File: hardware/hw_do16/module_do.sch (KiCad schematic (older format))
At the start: 130 parts, among them J1 DO_0, J2 DO_1, J3 MOD, P3 DEBUG, Q1 IRLML5103, Q10 IRLML5103, Q11 IRLML5103, Q12 IRLML5103, Q13 IRLML5103, Q14 IRLML5103, Q15 IRLML5103, Q16 IRLML5103, Q2 IRLML5103, Q3 IRLML5103, Q4 IRLML5103, Q5 IRLML5103, Q6 IRLML5103, Q7 IRLML5103, Q8 IRLML5103, Q9 IRLML5103, U1 STM32F103C8Tx, U2 TLP291-4, U3 TLP291-4, U4 TLP291-4, U5 TLP291-4

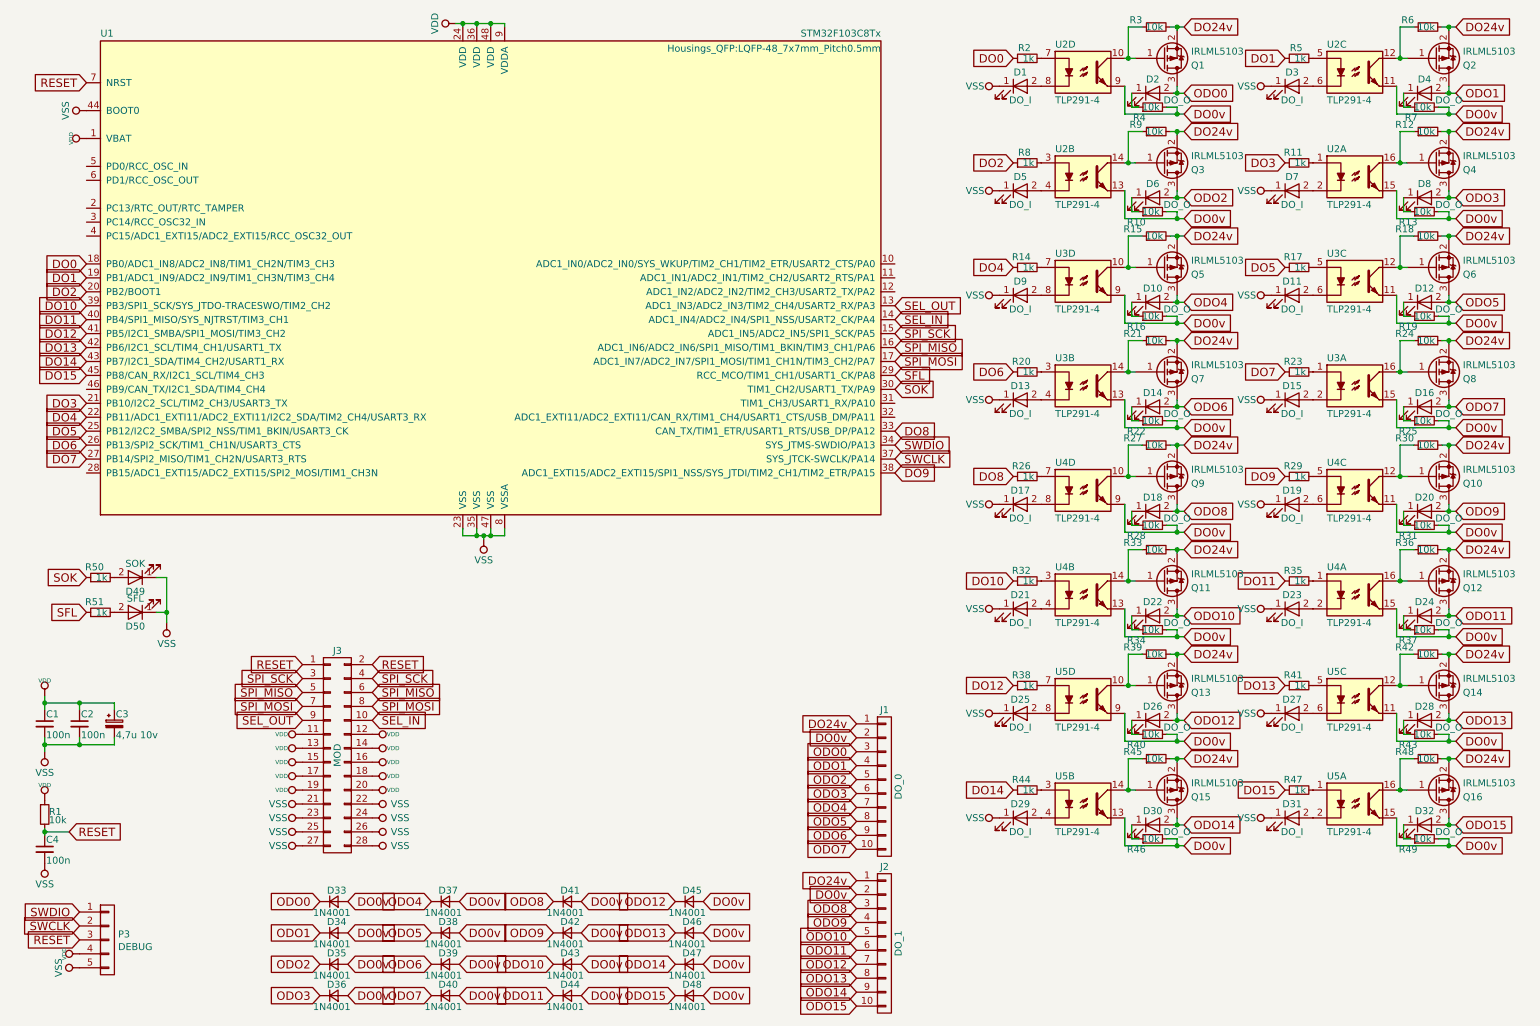
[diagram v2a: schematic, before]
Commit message: Обновлены платы модулей.
Добавлен разъем для работы с аппаратным загрузчиком.
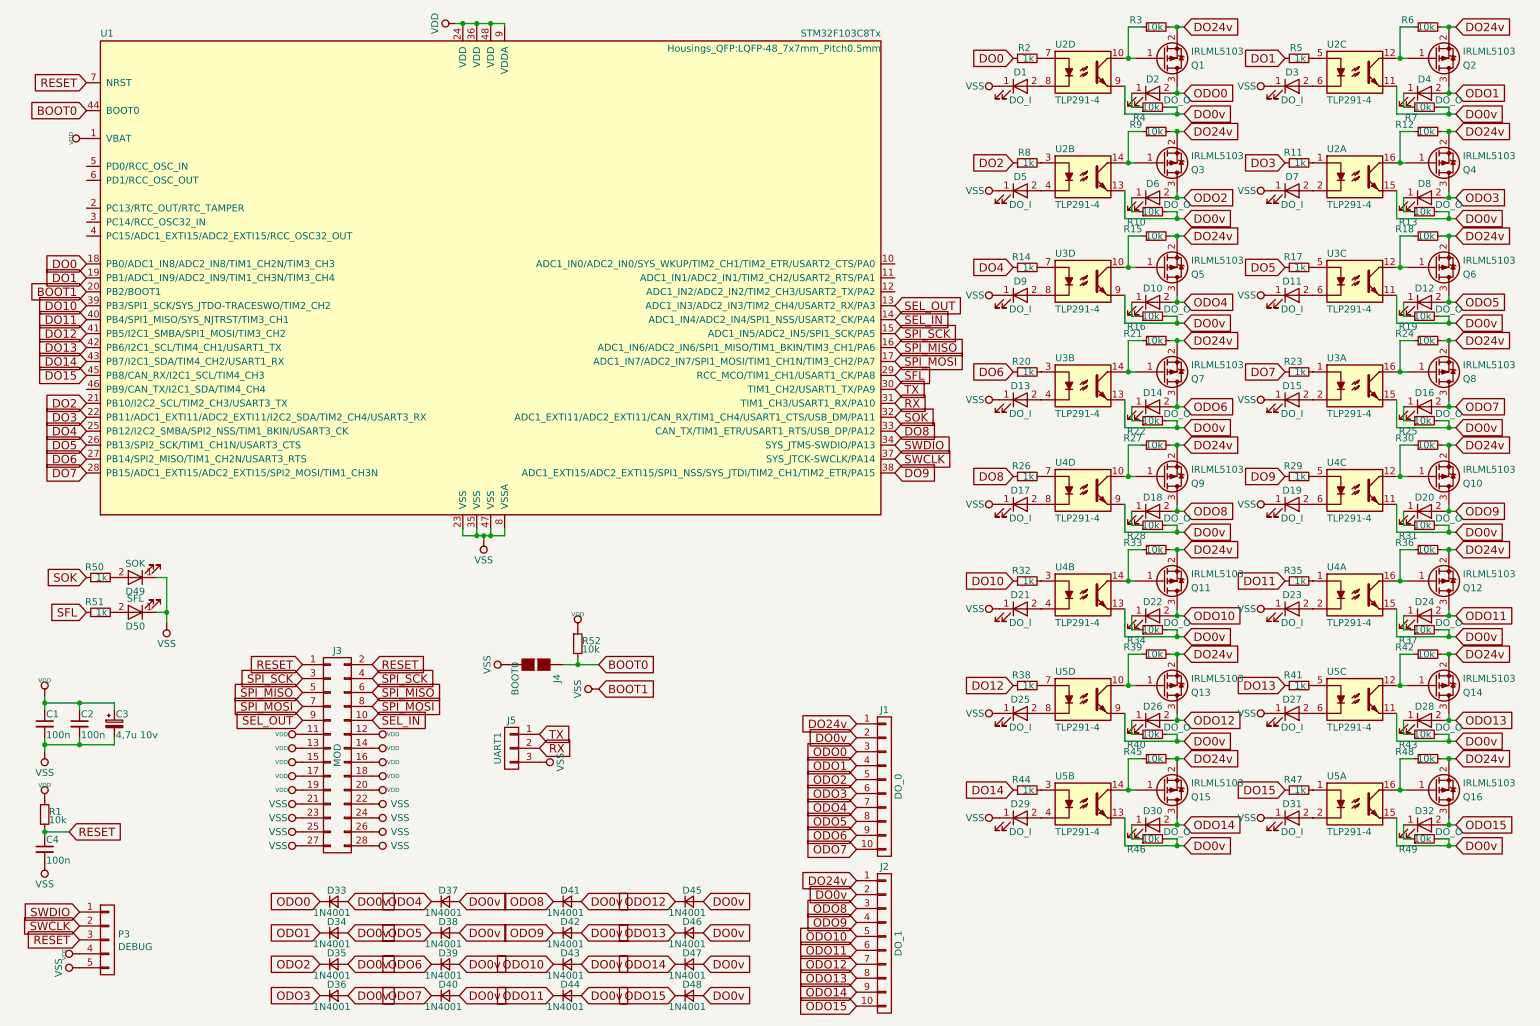
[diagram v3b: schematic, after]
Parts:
- added J4: BOOT0, Connect:GS2, symbol GS2
- added J5: UART1, Pin_Headers:Pin_Header_Straight_1x03_Pitch2.00mm, symbol CONN_01X03
- added R52: 10k, Resistors_SMD:R_0805, symbol R_Small
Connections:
- net DO2: now also U1.21 (PB10/I2C2_SCL/TIM2_CH3/USART3_TX); no longer U1.20 (PB2/BOOT1)
- net DO3: now also U1.22 (PB11/ADC1_EXTI11/ADC2_EXTI11/I2C2_SDA/TIM2_CH4/USART3_RX); no longer U1.21 (PB10/I2C2_SCL/TIM2_CH3/USART3_TX)
- net DO4: now also U1.25 (PB12/I2C2_SMBA/SPI2_NSS/TIM1_BKIN/USART3_CK); no longer U1.22 (PB11/ADC1_EXTI11/ADC2_EXTI11/I2C2_SDA/TIM2_CH4/USART3_RX)
- net DO5: now also U1.26 (PB13/SPI2_SCK/TIM1_CH1N/USART3_CTS); no longer U1.25 (PB12/I2C2_SMBA/SPI2_NSS/TIM1_BKIN/USART3_CK)
- net DO6: now also U1.27 (PB14/SPI2_MISO/TIM1_CH2N/USART3_RTS); no longer U1.26 (PB13/SPI2_SCK/TIM1_CH1N/USART3_CTS)
- net DO7: now also U1.28 (PB15/ADC1_EXTI15/ADC2_EXTI15/SPI2_MOSI/TIM1_CH3N); no longer U1.27 (PB14/SPI2_MISO/TIM1_CH2N/USART3_RTS)
- net SOK: now also U1.32 (ADC1_EXTI11/ADC2_EXTI11/CAN_RX/TIM1_CH4/USART1_CTS/USB_DM/PA11); no longer U1.30 (TIM1_CH2/USART1_TX/PA9)
- net VDD: now also R52.1
- net VSS: now also U1.20 (PB2/BOOT1), J4.2 (G2), J5.3 (P3); no longer U1.44 (BOOT0)
- net RX: now reaches U1.31 (TIM1_CH3/USART1_RX/PA10)
- net RX: now also J5.2 (P2)
- new net BOOT0: J4.1 (G1), R52.2, U1.44 (BOOT0)
- new net TX: J5.1 (P1), U1.30 (TIM1_CH2/USART1_TX/PA9)
